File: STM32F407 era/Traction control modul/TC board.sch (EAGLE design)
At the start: 10 parts, among them IC1 TL072D

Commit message: started work on traction control node
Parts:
- removed JP1, JP2: (no value), unicorn_v2:M02-JST-2MM-SMT
- removed R4, R5: (no value), microbuilder:RESISTOR0603
- added C3, C4: 100n, microbuilder:CAP_CERAMIC_0603
- added D1: 1n5824, diode:SCHOTTKY-DIODEF126Z12
- added H1, H2, H3, H4: MOUNT-HOLE3.0, holes:MOUNT-HOLE3.0
- added IC2: lm2575, linear:LM2596S
- added J1: (no value), unicorn_v2:AUTOCONNECTOR
- added L1: MSS1278-224KLD, SparkFun-Passives:INDUCTORPWR
- added U$1: CPU-BOARD, unicorn_v2:CPU-BOARD
- added U1: MAX13052ESA+, Maxim_By_element14_Batch_1:MAX13052ESA+
- C1: value (none) -> 100u; device microbuilder:CAP_CERAMIC0603 -> rcl:CPOL-EUE2.5-7
- C2: value (none) -> 220uf; device microbuilder:CAP_CERAMIC0603 -> rcl:CPOL-EUE3.5-8
- IC1: value TL072D -> 74HC14D; device linear:TL072D -> 74xx-eu:74HC14D
- R1: value (none) -> 1k; device microbuilder:RESISTOR0603 -> microbuilder:RESISTOR_0603
- R2: value (none) -> 1k69; device microbuilder:RESISTOR0603 -> microbuilder:RESISTOR_0603
- R3: value (none) -> 1k8; device microbuilder:RESISTOR0603 -> microbuilder:RESISTOR_0603
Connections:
- removed net N$7: IC1B.OUT, JP2.1, R5.1
- new net 12V: C1.+, IC2.IN, J1G$1.M
- new net 3.3V: C2.+, C3.P$1, C4.P$1, IC1P.VCC, J1G$1.E, J1G$2.E, J1G$3.E, J1G$4.E, L1.2, R2.1, U$1G$2.VCC1, U$1G$2.VCC2, U1.VCC
- new net CANH: R3.2, U1.CANL
- new net CANL: R3.1, U1.CANH
- new net CAN_RX: U$1G$3.PB5, U1.TXD
- new net CAN_TX: U$1G$3.PB6, U1.RXD
- new net N$6: IC1C.I, J1G$3.B
- new net RPM1: IC1D.O, U$1G$3.PC10
- new net RPM2: IC1C.O, U$1G$3.PC11
- new net RPM3: IC1B.O, U$1G$3.PC12
- new net RPM4: IC1A.O, U$1G$3.PD2
- new net TRAVEL1: J1G$2.D, U$1G$1.PA3
- new net TRAVEL2: J1G$1.D, U$1G$1.PA5
- new net TRAVEL3: J1G$3.D, U$1G$1.PA7
- new net TRAVEL4: J1G$4.D, U$1G$1.PC5
- net GND: now also C1.-, C2.-, C3.P$2, C4.P$2, D1.A, IC1P.GND, IC2.EN, IC2.GND, IC2.GND@1, J1G$1.C, J1G$1.L, J1G$2.A, J1G$2.B, J1G$2.C, J1G$3.C, J1G$4.A, J1G$4.B, J1G$4.C, R1.1, U$1G$1.GND1, U$1G$1.GND2, U$1G$2.GND3, U$1G$2.GND4, U$1G$3.GND5, U$1G$4.GND6, U$1G$4.GND7, U$1G$4.GND8, U1.GND, U1.RS; no longer C2.P$1, IC1B.-IN, R2.2, R5.2
- net N$1: now also IC2.FB, R1.2, R2.2; no longer JP1.1, R4.2
- net N$2: now also D1.C, IC2.OUT, L1.1; no longer C1.P$1, R3.2, R4.1
- net N$3: now also IC1B.I, J1G$1.A; no longer IC1A.+IN, R3.1
- net N$4: now also IC1A.I, J1G$1.B; no longer C1.P$2, IC1A.OUT, IC1B.+IN, R1.1
- net N$5: now also IC1D.I, J1G$3.A; no longer IC1A.-IN, R1.2, R2.1
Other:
- moved on the sheet: R1, R2, R3

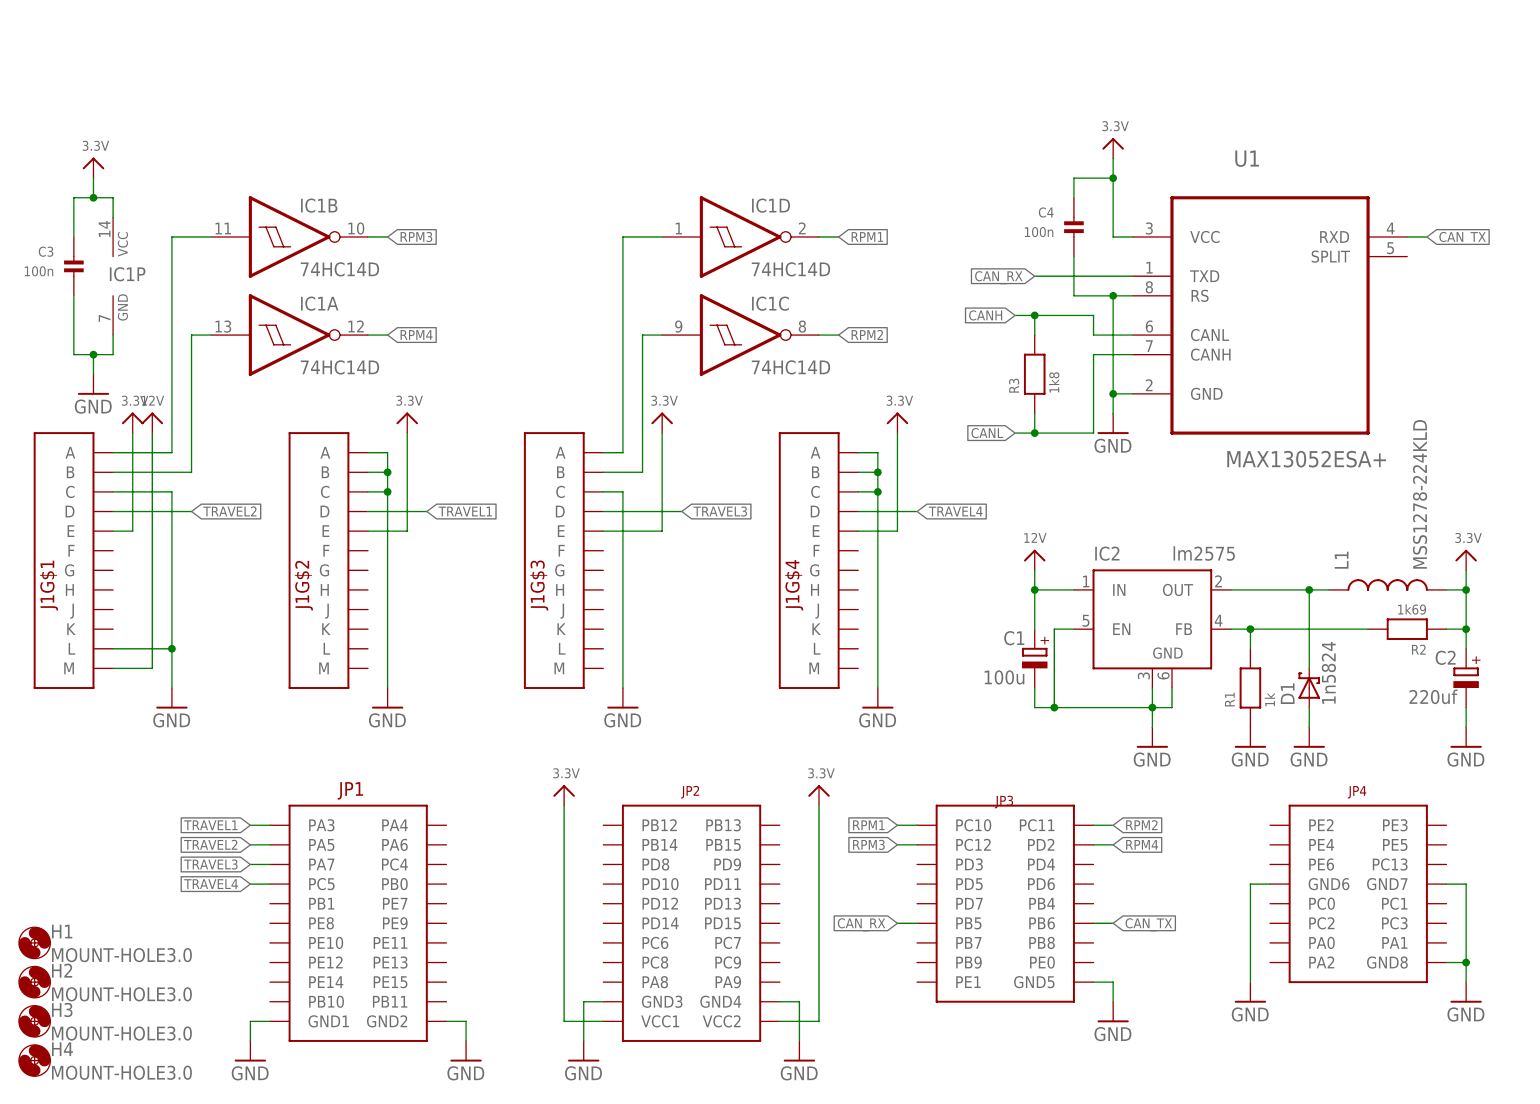
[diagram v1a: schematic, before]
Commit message: more work on TC, startet work on Aux sensor board
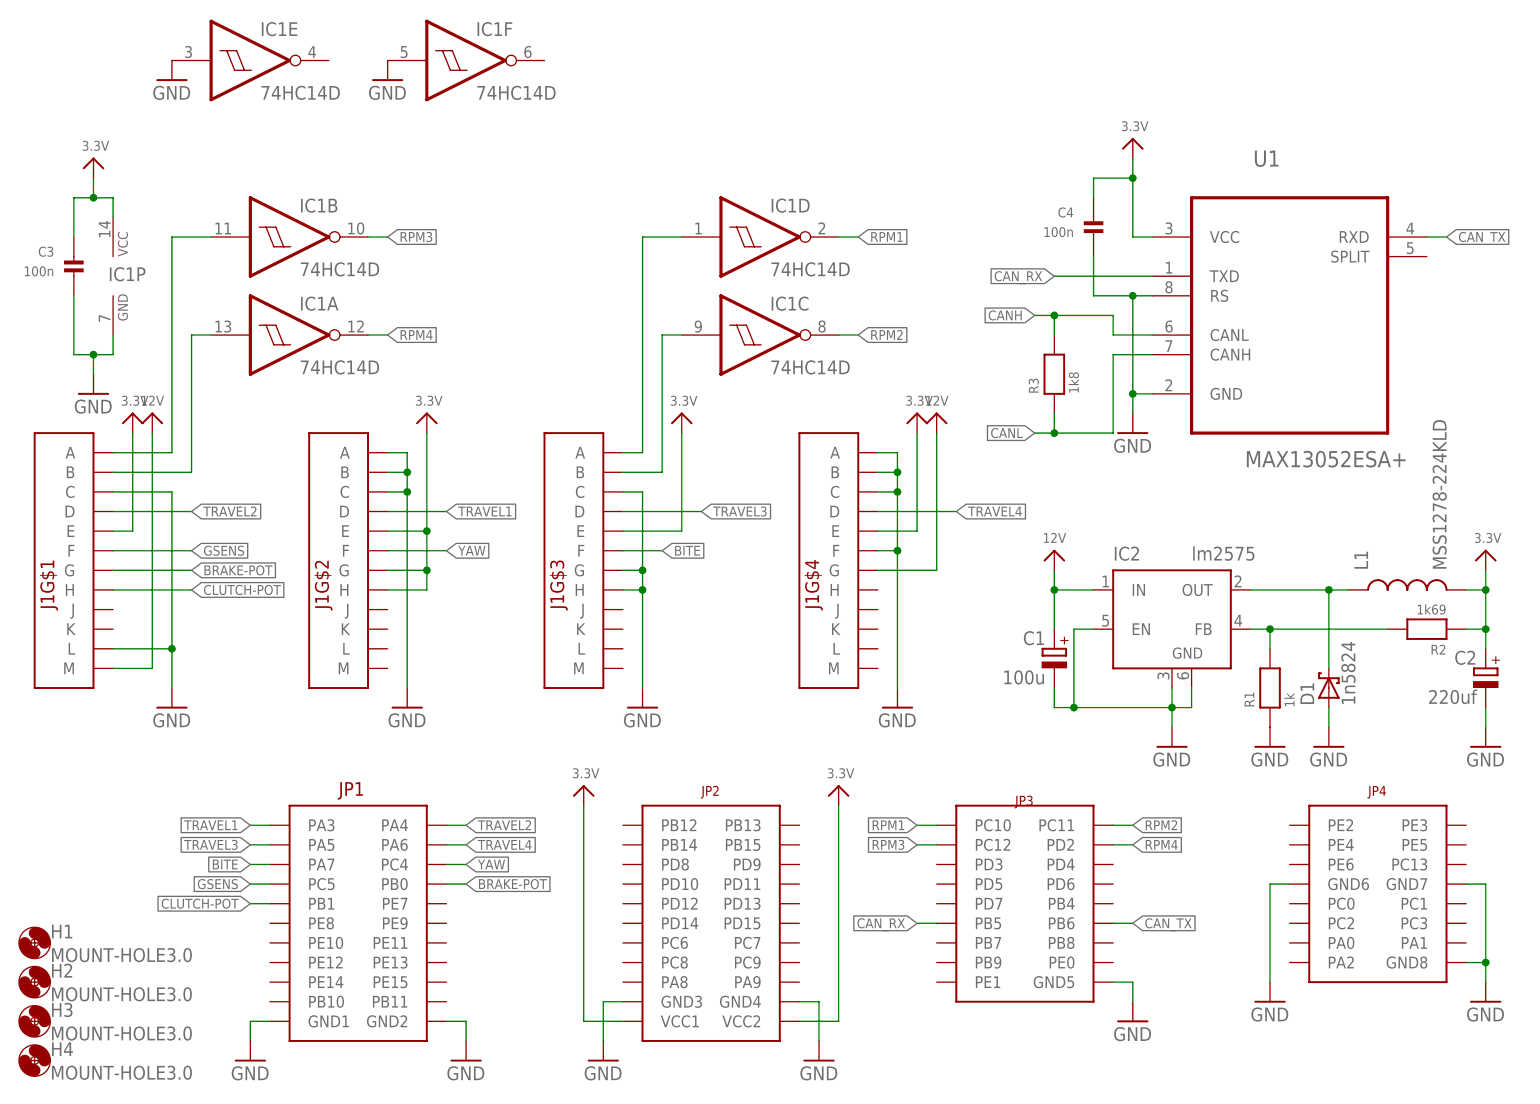
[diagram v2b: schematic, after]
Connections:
- new net BITE: J1G$3.F, U$1G$1.PA7
- new net BRAKE-POT: J1G$1.G, U$1G$1.PB0
- new net CLUTCH-POT: J1G$1.H, U$1G$1.PB1
- new net GSENS: J1G$1.F, U$1G$1.PC5
- new net YAW: J1G$2.F, U$1G$1.PC4
- net 12V: now also J1G$4.G
- net 3.3V: now also J1G$2.G, J1G$2.H
- net GND: now also IC1E.I, IC1F.I, J1G$3.G, J1G$3.H, J1G$4.F
- net TRAVEL2: now also U$1G$1.PA4; no longer U$1G$1.PA5
- net TRAVEL3: now also U$1G$1.PA5; no longer U$1G$1.PA7
- net TRAVEL4: now also U$1G$1.PA6; no longer U$1G$1.PC5
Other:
- moved on the sheet: C1, C2, C4, D1, IC1C, IC1D, IC2, J1G$2, J1G$3, J1G$4, L1, R1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

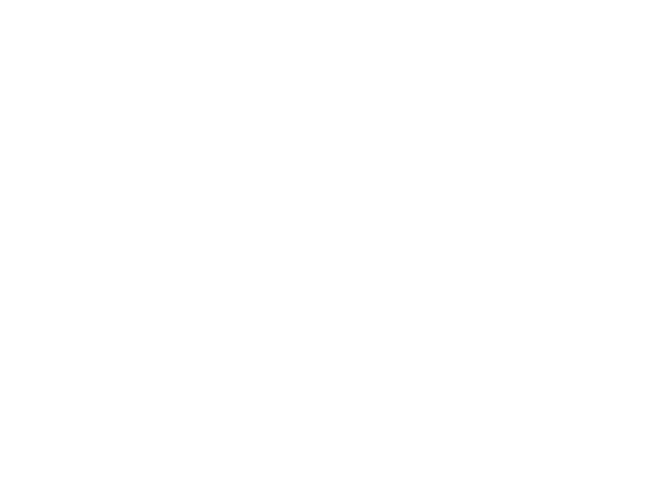
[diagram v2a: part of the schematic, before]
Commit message: merged TC board with AUX board
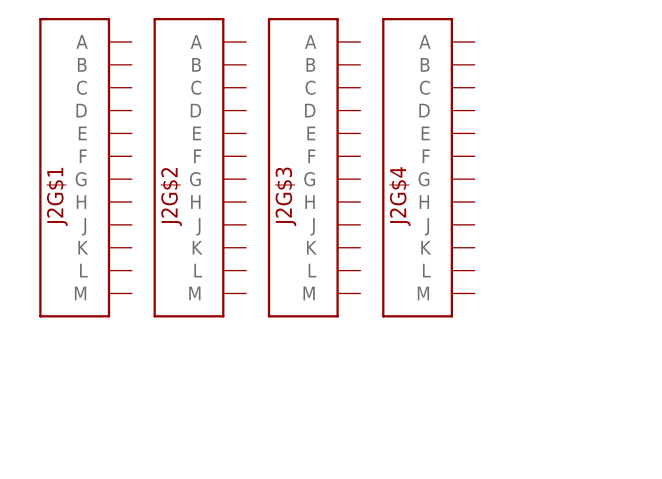
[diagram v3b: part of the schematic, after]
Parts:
- added J2: (no value), unicorn_v2:AUTOCONNECTOR
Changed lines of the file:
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@@
 <part name="GND18" library="supply1" deviceset="GND" device=""/>
 <part name="GND19" library="supply1" deviceset="GND" device=""/>
+<part name="J2" library="unicorn_v2" deviceset="AUTOCONNECTOR" device=""/>
 </parts>
 <sheets>
@@
 <instance part="GND18" gate="1" x="20.32" y="129.54"/>
 <instance part="GND19" gate="1" x="48.26" y="129.54"/>
+<instance part="J2" gate="G$1" x="7.62" y="172.72"/>
+<instance part="J2" gate="G$2" x="20.32" y="172.72"/>
+<instance part="J2" gate="G$3" x="33.02" y="172.72"/>
+<instance part="J2" gate="G$4" x="45.72" y="172.72"/>
 </instances>
 <busses>

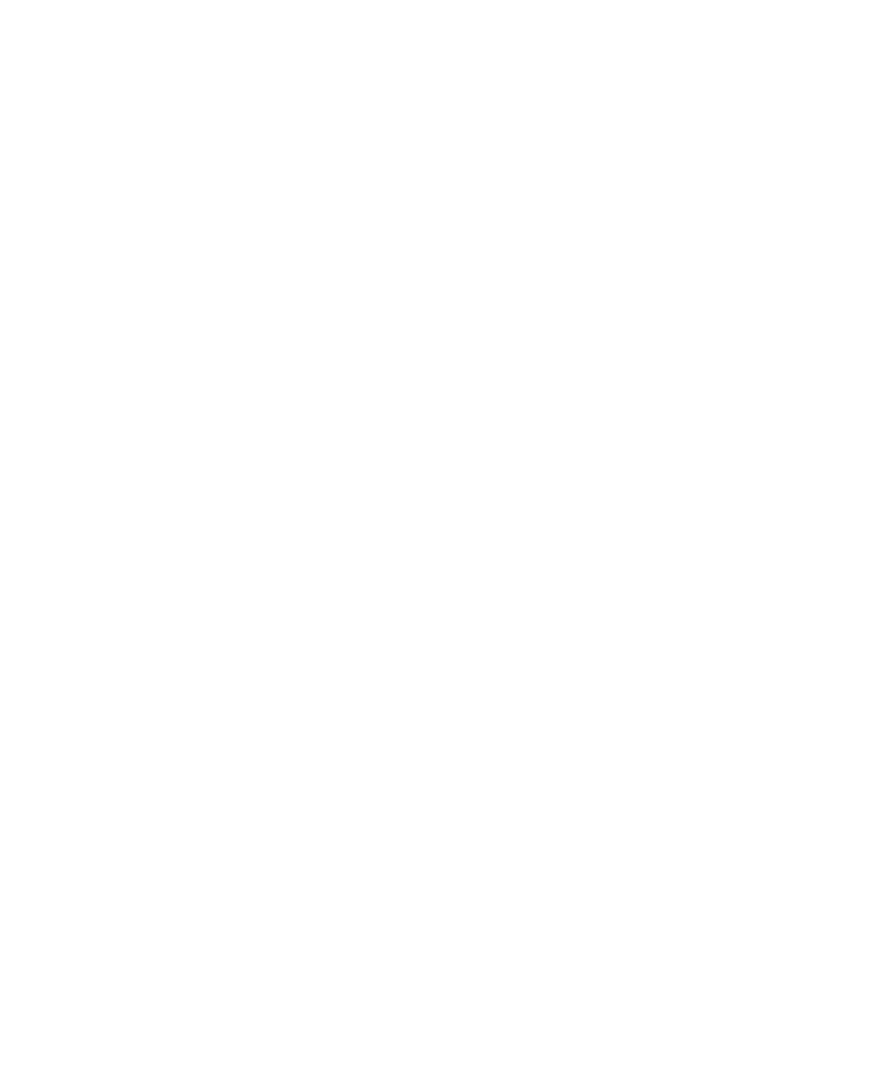
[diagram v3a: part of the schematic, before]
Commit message: started working on control signals to gear
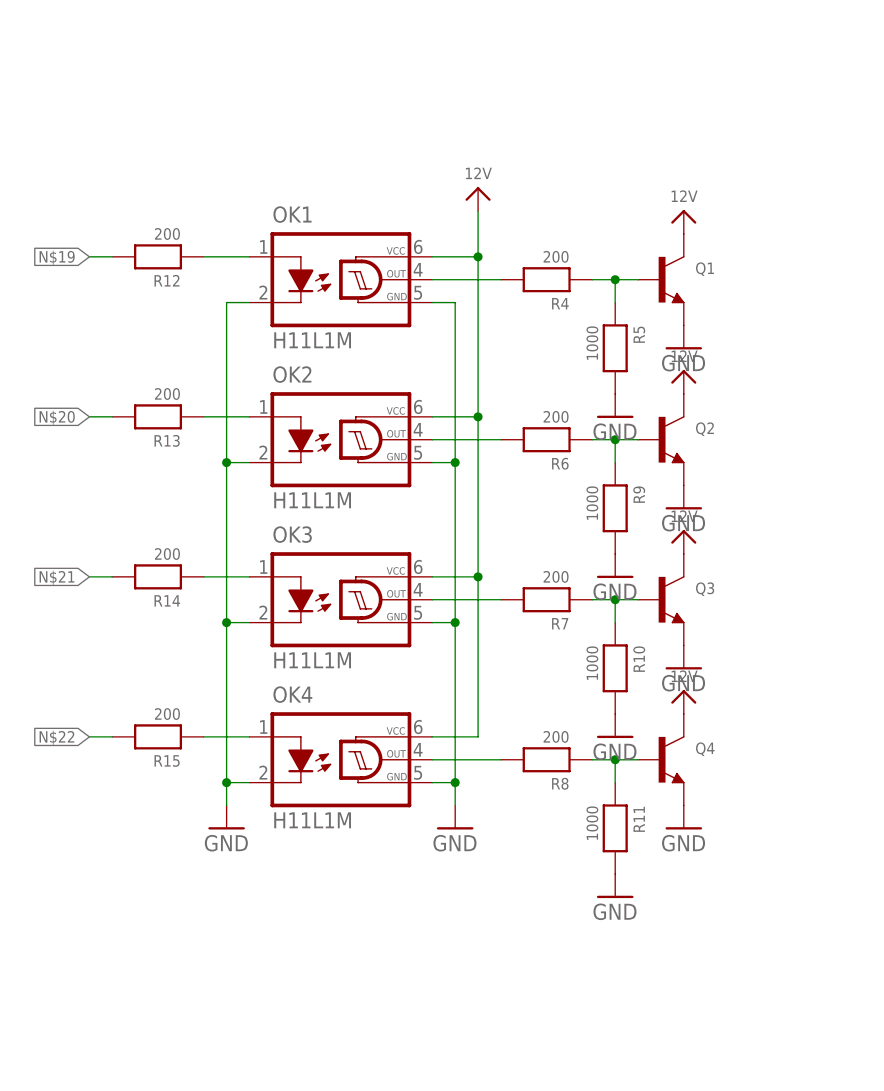
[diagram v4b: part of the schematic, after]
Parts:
- added OK1, OK2, OK3, OK4: H11L1M, optocoupler:H11L1M
- added Q1, Q2, Q3, Q4: (no value), microbuilder:TRANSISTOR_NPNWIDE
- added R10, R11, R5, R9: 1000, microbuilder:RESISTOR_0603
- added R12, R13, R14, R15, R4, R6, R7, R8: 200, microbuilder:RESISTOR_0603
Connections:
- new net N$10: Q2.B, R6.1, R9.1
- new net N$11: OK3.OUT, R7.2
- new net N$12: Q3.B, R10.1, R7.1
- new net N$13: OK4.OUT, R8.2
- new net N$14: Q4.B, R11.1, R8.1
- new net N$15: OK4.A, R15.1
- new net N$16: OK3.A, R14.1
- new net N$17: OK2.A, R13.1
- new net N$18: OK1.A, R12.1
- new net N$19: R12.2
- new net N$20: R13.2
- new net N$21: R14.2
- new net N$22: R15.2
- new net N$7: OK1.OUT, R4.2
- new net N$8: Q1.B, R4.1, R5.1
- new net N$9: OK2.OUT, R6.2
- net 12V: now also OK1.VCC, OK2.VCC, OK3.VCC, OK4.VCC, Q1.C, Q2.C, Q3.C, Q4.C
- net GND: now also OK1.C, OK1.GND, OK2.C, OK2.GND, OK3.C, OK3.GND, OK4.C, OK4.GND, Q1.E, Q2.E, Q3.E, Q4.E, R10.2, R11.2, R5.2, R9.2

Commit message: succeded in removing one of 2 connectors
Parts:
- removed J2: (no value), unicorn_v2:AUTOCONNECTOR
- removed OK1, OK2: H11L1M, optocoupler:H11L1M
- removed Q4: (no value), microbuilder:TRANSISTOR_NPNWIDE
- added C10, C11, C12, C5, C6, C8, C9: 100n, microbuilder:CAP_CERAMIC_0603
- added C7: 4n7, microbuilder:CAP_CERAMIC_0603
- added IC3: 74AC08D, 74xx-eu:74AC08D
- added IC4: 74AC04D, 74xx-eu:74AC04D
- added R16: 178, microbuilder:RESISTOR_0603
- added R17: 500, microbuilder:RESISTOR_0603
- added U2: MAX232AEWE+, Maxim_By_element14_Batch_1:MAX232AEWE+
- added X1: 057-006-1, con-panduit:057-006-1
- J1: value (none) -> CON1
- OK3, OK4: value H11L1M -> 4N37; device optocoupler:H11L1M -> optocoupler:4N37
- R10: value 1000 -> 178
- R11: value 1000 -> 604
- R14: value 200 -> 178
- R15, R8: value 200 -> 604
- R3: value 1k8 -> 60
- R7: value 200 -> 60
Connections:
- new net BITEO: R15.1, R16.2, U$1G$1.PA7
- new net BRAKEP: J1G$1.K, U$1G$4.PA1
- new net COMRX: U2.R2OUT, X1-1.S
- new net COMTX: U2.T2IN, X1-2.S
- new net DIRA: IC3A.I0, IC4B.I, U$1G$2.PA8
- new net DIRAO: J1G$3.L, Q1.E
- new net DIRB: IC3B.I1, IC4A.I, U$1G$2.PA9
- new net DIRBO: J1G$3.M, Q2.E
- new net FUEL1: J1G$3.J
- new net FUEL2: J1G$3.K
- new net FUEL3: J1G$4.J
- new net FUEL4: J1G$4.K
- new net GSENSO: R10.2, R8.1, U$1G$1.PC5
- new net IGNCUT: R17.2, U$1G$1.PE7
- new net IGNCUTO: J1G$4.H, Q3.C
- new net N$23: C11.P$1, U2.V+
- new net N$24: Q3.B, R17.1
- new net NEUTRAL: J1G$1.J, U$1G$1.PE8
- new net OILP: J1G$2.J, U$1G$1.PE9
- new net RS232RX: J1G$1.M, U2.R2IN
- new net RS232TX: J1G$1.L, U2.T2OUT
- new net SPEED: J1G$2.G, U$1G$4.PA2
- new net VTEMP: J1G$1.H, U$1G$4.PA0
- new net VTEMP2: J1G$3.H, U$1G$4.PC3
- new net YAWO: R11.1, R14.2, U$1G$1.PC4
- net 12V: now also J1G$4.F, J1G$4.M, OK3.COL, OK4.COL, X1-5.S; no longer J1G$1.M, J1G$4.G, OK1.VCC, OK2.VCC, OK3.VCC, OK4.VCC, Q3.C, Q4.C
- net 3.3V: now also C10.P$2, C5.P$1, C6.P$1, IC3P.VCC, IC4P.VCC, J1G$1.D, J1G$2.D, J1G$2.F, J1G$3.D, J1G$4.D, J1G$4.G, U2.VCC; no longer J1G$1.E, J1G$2.E, J1G$2.G, J1G$2.H, J1G$3.E, J1G$4.E
- net BITE: now also J1G$3.E, R15.2; no longer J1G$3.F, U$1G$1.PA7
- net BRAKE-POT: now also J1G$1.F; no longer J1G$1.G
- net CANH: now also R7.1, X1-3.S; no longer R3.2
- net CANL: now also X1-4.S
- net CAN_RX: now also U1.RXD; no longer U1.TXD
- net CAN_TX: now also U1.TXD; no longer U1.RXD
- net CLUTCH-POT: now also J1G$1.G; no longer J1G$1.H
- net GND: now also C10.P$1, C11.P$2, C12.P$1, C5.P$2, C6.P$2, C7.P$2, IC3C.I0, IC3C.I1, IC3D.I0, IC3D.I1, IC3P.GND, IC4C.I, IC4D.I, IC4E.I, IC4F.I, IC4P.GND, J1G$1.B, J1G$2.H, J1G$3.B, J1G$3.F, J1G$4.E, J1G$4.L, R10.1, R14.1, R16.1, U2.GND, X1-6.S; no longer J1G$1.C, J1G$1.L, J1G$2.A, J1G$2.C, J1G$3.C, J1G$3.H, J1G$4.A, J1G$4.C, J1G$4.F, OK1.C, OK1.GND, OK2.C, OK2.GND, OK3.GND, OK4.GND, Q1.E, Q2.E, Q4.E, R10.2, R11.2
- net GSENS: now also J1G$1.E, R8.2; no longer J1G$1.F, U$1G$1.PC5
- net N$11: now also IC3B.O, R13.2; no longer OK3.OUT, R7.2
- net N$12: now also C7.P$1, R3.2, R7.2, U1.SPLIT; no longer Q3.B, R10.1, R7.1
- net N$13: now also C12.P$2, U2.V-; no longer OK4.OUT, R8.2
- net N$14: now also C9.P$1, U2.C2+; no longer Q4.B, R11.1, R8.1
- net N$15: now also IC3B.I0, IC4B.O; no longer OK4.A, R15.1
- net N$16: now also IC3A.I1, IC4A.O; no longer OK3.A, R14.1
- net N$17: now also OK4.A; no longer OK2.A
- net N$18: now also OK3.A; no longer OK1.A
- net N$19: now also IC3A.O
- net N$20: now also C9.P$2, U2.C2-; no longer R13.2
- net N$21: now also C8.P$2, U2.C1-; no longer R14.2
- net N$22: now also C8.P$1, U2.C1+; no longer R15.2
- net N$3: now also IC1C.I, J1G$3.A; no longer IC1B.I, J1G$1.A
- net N$4: now also J1G$1.A; no longer J1G$1.B
- net N$5: now also J1G$4.A; no longer J1G$3.A
- net N$6: now also IC1B.I, J1G$2.A; no longer IC1C.I, J1G$3.B
- net N$7: now also OK3.EMI; no longer OK1.OUT
- net N$9: now also OK4.EMI; no longer OK2.OUT
- net TRAVEL1: now also J1G$2.C; no longer J1G$2.D
- net TRAVEL2: now also J1G$1.C; no longer J1G$1.D
- net TRAVEL3: now also J1G$3.C; no longer J1G$3.D
- net TRAVEL4: now also J1G$4.C; no longer J1G$4.D
- net YAW: now also J1G$2.E, R11.2; no longer J1G$2.F, U$1G$1.PC4
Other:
- note added: "14V to 3,3V voltage dividers"
- note added: "CAN Transciever"
- note added: "COM - TC interconnect"
- note added: "CPU Board"
- note added: "Connector 1"
- note added: "Gear control signal"
- note added: "Ignition cut"
- note added: "Power Supply"
- note added: "RS232 Transciever"
- moved on the sheet: C1, C2, C3, C4, D1, H1, H2, H3, H4, IC1A, IC1B, IC1C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
